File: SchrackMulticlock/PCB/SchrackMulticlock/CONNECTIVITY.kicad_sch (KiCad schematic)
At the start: 26 parts, among them J1 TYPE-C-31-M-12 (USB C CONN), U7 USBLC6-2SC6

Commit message: SchrackMulticlock update
Schematic and PCB update
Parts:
- D4: footprint LED_SMD:LED_Cree-PLCC4_3.2x2.8mm_CCW -> LED_THT:LED_D5.0mm
- D5, D6, D7: footprint LED_SMD:LED_0805_2012Metric_Pad1.15x1.40mm_HandSolder -> LED_THT:LED_D5.0mm
- gave numbers to parts that had none: 2
- renumbered C9 to C10, R9 to R10, R10 to R11, R11 to R12, R5 to R6, R6 to R7, R7 to R8, R8 to R9
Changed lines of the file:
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@@
 			)
 		)
-		(property "Footprint" "LED_SMD:LED_0805_2012Metric_Pad1.15x1.40mm_HandSolder"
+		(property "Footprint" "LED_THT:LED_D5.0mm"
 			(at 217.17 121.92 0)
 			(effects
@@
 		(dnp no)
 		(fields_autoplaced yes)
-		(property "Reference" "#PWR0120"
+		(property "Reference" "#PWR022"
 			(at 173.99 62.23 0)
 			(effects
@@
 			(project "SchrackCounter"
 				(path "/d96f2ffc-3f4c-4f71-b693-29f6b8c3245d/301b3ab9-8372-40d2-93c7-cd7607d23fc4"
-					(reference "#PWR0120")
+					(reference "#PWR022")
 					(unit 1)
 				)
@@
 			)
 		)
-		(property "Footprint" "LED_SMD:LED_0805_2012Metric_Pad1.15x1.40mm_HandSolder"
+		(property "Footprint" "LED_THT:LED_D5.0mm"
 			(at 217.17 135.89 0)
 			(effects
@@
 		(dnp no)
 		(fields_autoplaced yes)
-		(property "Reference" "#PWR0118"
+		(property "Reference" "#PWR024"
 			(at 224.79 132.08 0)
 			(effects
@@
 			(project "SchrackMulticlock"
 				(path "/d96f2ffc-3f4c-4f71-b693-29f6b8c3245d/301b3ab9-8372-40d2-93c7-cd7607d23fc4"
-					(reference "#PWR0118")
+					(reference "#PWR024")
 					(unit 1)
 				)
@@
 		(dnp no)
 		(fields_autoplaced yes)
-		(property "Reference" "#PWR0121"
+		(property "Reference" "#PWR021"
 			(at 179.07 142.24 0)
 			(effects
@@
 			(project "SchrackCounter"
 				(path "/d96f2ffc-3f4c-4f71-b693-29f6b8c3245d/301b3ab9-8372-40d2-93c7-cd7607d23fc4"
-					(reference "#PWR0121")
+					(reference "#PWR021")
 					(unit 1)
 				)
@@
 		(dnp no)
 		(fields_autoplaced yes)
-		(property "Reference" "#PWR0122"
+		(property "Reference" "#PWR020"
 			(at 179.07 128.27 0)
 			(effects
@@
 			(project "SchrackCounter"
 				(path "/d96f2ffc-3f4c-4f71-b693-29f6b8c3245d/301b3ab9-8372-40d2-93c7-cd7607d23fc4"
-					(reference "#PWR0122")
+					(reference "#PWR020")
 					(unit 1)
 				)
@@
 		(dnp no)
 		(fields_autoplaced yes)
-		(property "Reference" "#PWR0113"
+		(property "Reference" "#PWR017"
 			(at 121.92 85.09 0)
 			(effects
@@
 			(project "SchrackCounter"
 				(path "/d96f2ffc-3f4c-4f71-b693-29f6b8c3245d/301b3ab9-8372-40d2-93c7-cd7607d23fc4"
-					(reference "#PWR0113")
+					(reference "#PWR017")
 					(unit 1)
 				)
@@
 		(on_board yes)
 		(dnp no)
-		(property "Reference" "#PWR0123"
+		(property "Reference" "#PWR019"
 			(at 160.02 121.92 0)
 			(effects
@@
 			(project "SchrackCounter"
 				(path "/d96f2ffc-3f4c-4f71-b693-29f6b8c3245d/301b3ab9-8372-40d2-93c7-cd7607d23fc4"
-					(reference "#PWR0123")
+					(reference "#PWR019")
 					(unit 1)
 				)
@@
 		(on_board yes)
 		(dnp no)
-		(property "Reference" "R9"
+		(property "Reference" "R10"
 			(at 173.99 72.39 90)
 			(effects
@@
 			(project "SchrackCounter"
 				(path "/d96f2ffc-3f4c-4f71-b693-29f6b8c3245d/301b3ab9-8372-40d2-93c7-cd7607d23fc4"
-					(reference "R9")
+					(reference "R10")
 					(unit 1)
 				)
@@
 		(dnp no)
 		(fields_autoplaced yes)
-		(property "Reference" "#PWR0117"
+		(property "Reference" "#PWR025"
 			(at 224.79 156.21 0)
 			(effects
@@
 			(project "SchrackMulticlock"
 				(path "/d96f2ffc-3f4c-4f71-b693-29f6b8c3245d/301b3ab9-8372-40d2-93c7-cd7607d23fc4"
-					(reference "#PWR0117")
+					(reference "#PWR025")
 					(unit 1)
 				)
@@
 		(on_board yes)
 		(dnp no)
-		(property "Reference" "R5"
+		(property "Reference" "R6"
 			(at 134.62 128.905 0)
 			(effects
@@
 			(project "SchrackCounter"
 				(path "/d96f2ffc-3f4c-4f71-b693-29f6b8c3245d/301b3ab9-8372-40d2-93c7-cd7607d23fc4"
-					(reference "R5")
+					(reference "R6")
 					(unit 1)
 				)
@@
 		(on_board yes)
 		(dnp no)
-		(property "Reference" "C?"
+		(property "Reference" "C9"
 			(at 113.03 72.39 0)
 			(effects
@@
 			(project "SchrackMulticlock"
 				(path "/d96f2ffc-3f4c-4f71-b693-29f6b8c3245d/301b3ab9-8372-40d2-93c7-cd7607d23fc4"
-					(reference "C?")
+					(reference "C9")
 					(unit 1)
 				)
@@
 		(dnp no)
 		(fields_autoplaced yes)
-		(property "Reference" "#PWR0124"
+		(property "Reference" "#PWR018"
 			(at 142.24 142.24 0)
 			(effects
@@
 			(project "SchrackCounter"
 				(path "/d96f2ffc-3f4c-4f71-b693-29f6b8c3245d/301b3ab9-8372-40d2-93c7-cd7607d23fc4"
-					(reference "#PWR0124")
+					(reference "#PWR018")
 					(unit 1)
 				)
@@
 		(on_board yes)
 		(dnp no)
-		(property "Reference" "R8"
+		(property "Reference" "R9"
 			(at 173.99 46.99 90)
 			(effects
@@
 			(project "SchrackCounter"
 				(path "/d96f2ffc-3f4c-4f71-b693-29f6b8c3245d/301b3ab9-8372-40d2-93c7-cd7607d23fc4"
-					(reference "R8")
+					(reference "R9")
 					(unit 1)
 				)
@@
 		(on_board yes)
 		(dnp no)
-		(property "Reference" "#PWR0115"
+		(property "Reference" "#PWR014"
 			(at 87.63 139.7 0)
 			(effects
@@
 			(project "SchrackCounter"
 				(path "/d96f2ffc-3f4c-4f71-b693-29f6b8c3245d/301b3ab9-8372-40d2-93c7-cd7607d23fc4"
-					(reference "#PWR0115")
+					(reference "#PWR014")
 					(unit 1)
 				)
@@
 		(on_board yes)
 		(dnp no)
-		(property "Reference" "R11"
+		(property "Reference" "R12"
 			(at 201.93 136.525 90)
 			(effects
@@
 			(project "SchrackMulticlock"
 				(path "/d96f2ffc-3f4c-4f71-b693-29f6b8c3245d/301b3ab9-8372-40d2-93c7-cd7607d23fc4"
-					(reference "R11")
+					(reference "R12")
 					(unit 1)
 				)
@@
 		(on_board yes)
 		(dnp no)
-		(property "Reference" "R?"
+		(property "Reference" "R5"
 			(at 105.41 72.39 0)
 			(effects
@@
 			(project "SchrackMulticlock"
 				(path "/d96f2ffc-3f4c-4f71-b693-29f6b8c3245d/301b3ab9-8372-40d2-93c7-cd7607d23fc4"
-					(reference "R?")
+					(reference "R5")
 					(unit 1)
 				)
@@
 		(on_board yes)
 		(dnp no)
-		(property "Reference" "#PWR0116"
+		(property "Reference" "#PWR013"
 			(at 87.63 127 0)
 			(effects
@@
 			(project "SchrackCounter"
 				(path "/d96f2ffc-3f4c-4f71-b693-29f6b8c3245d/301b3ab9-8372-40d2-93c7-cd7607d23fc4"
-					(reference "#PWR0116")
+					(reference "#PWR013")
 					(unit 1)
 				)
@@
 		(on_board yes)
 		(dnp no)
-		(property "Reference" "#PWR0114"
+		(property "Reference" "#PWR015"
 			(at 87.63 151.13 0)
 			(effects
@@
 			(project "SchrackCounter"
 				(path "/d96f2ffc-3f4c-4f71-b693-29f6b8c3245d/301b3ab9-8372-40d2-93c7-cd7607d23fc4"
-					(reference "#PWR0114")
+					(reference "#PWR015")
 					(unit 1)
 				)
@@
 			)
 		)
-		(property "Footprint" "LED_SMD:LED_0805_2012Metric_Pad1.15x1.40mm_HandSolder"
+		(property "Footprint" "LED_THT:LED_D5.0mm"
 			(at 217.17 146.05 0)
 			(effects
@@
 		(on_board yes)
 		(dnp no)
-		(property "Reference" "R6"
+		(property "Reference" "R7"
 			(at 172.72 117.475 90)
 			(effects
@@
 			(project "SchrackCounter"
 				(path "/d96f2ffc-3f4c-4f71-b693-29f6b8c3245d/301b3ab9-8372-40d2-93c7-cd7607d23fc4"
-					(reference "R6")
+					(reference "R7")
 					(unit 1)
 				)
@@
 		(on_board yes)
 		(dnp no)
-		(property "Reference" "C9"
+		(property "Reference" "C10"
 			(at 227.33 66.04 0)
 			(effects
@@
 			(project "SchrackCounter"
 				(path "/d96f2ffc-3f4c-4f71-b693-29f6b8c3245d/301b3ab9-8372-40d2-93c7-cd7607d23fc4"
-					(reference "C9")
+					(reference "C10")
 					(unit 1)
 				)
@@
 		(dnp no)
 		(fields_autoplaced yes)
-		(property "Reference" "#PWR01"
+		(property "Reference" "#PWR016"
 			(at 118.11 85.09 0)
 			(effects
@@
 			(project "SchrackMulticlock"
 				(path "/d96f2ffc-3f4c-4f71-b693-29f6b8c3245d/301b3ab9-8372-40d2-93c7-cd7607d23fc4"
-					(reference "#PWR01")
+					(reference "#PWR016")
 					(unit 1)
 				)
@@
 		(dnp no)
 		(fields_autoplaced yes)
-		(property "Reference" "#PWR0119"
+		(property "Reference" "#PWR023"
 			(at 223.52 76.2 0)
 			(effects
@@
 			(project "SchrackCounter"
 				(path "/d96f2ffc-3f4c-4f71-b693-29f6b8c3245d/301b3ab9-8372-40d2-93c7-cd7607d23fc4"
-					(reference "#PWR0119")
+					(reference "#PWR023")
 					(unit 1)
 				)
@@
 		(on_board yes)
 		(dnp no)
-		(property "Reference" "R7"
+		(property "Reference" "R8"
 			(at 172.72 131.445 90)
 			(effects
@@
 			(project "SchrackCounter"
 				(path "/d96f2ffc-3f4c-4f71-b693-29f6b8c3245d/301b3ab9-8372-40d2-93c7-cd7607d23fc4"
-					(reference "R7")
+					(reference "R8")
 					(unit 1)
 				)
@@
 		(on_board yes)
 		(dnp no)
-		(property "Reference" "R10"
+		(property "Reference" "R11"
 			(at 201.93 112.395 90)
 			(effects
@@
 			(project "SchrackMulticlock"
 				(path "/d96f2ffc-3f4c-4f71-b693-29f6b8c3245d/301b3ab9-8372-40d2-93c7-cd7607d23fc4"
-					(reference "R10")
+					(reference "R11")
 					(unit 1)
 				)
@@
 			)
 		)
-		(property "Footprint" "LED_SMD:LED_Cree-PLCC4_3.2x2.8mm_CCW"
+		(property "Footprint" "LED_THT:LED_D5.0mm"
 			(at 217.17 111.76 0)
 			(effects
@@
 			)
 		)
-		(property "Datasheet" "~"
+		(property "Datasheet" "https://cz.mouser.com/ProductDetail/Cree-LED/CLM2B-REW-CYaZ0AA3?qs=3AcK5DacLboBP3rYC%2FbEBg%3D%3D"
 			(at 217.17 111.76 0)
 			(effects

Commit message: SchrackCounter update - FIX
USB footprint standoff fix
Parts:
- J1: footprint sumec_brd:USB_Type_C -> Connector_USB:USB_C_Receptacle_GCT_USB4105-xx-A_16P_TopMnt_Horizontal
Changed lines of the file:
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@@
 			)
 		)
-		(property "Footprint" "sumec_brd:USB_Type_C"
+		(property "Footprint" "Connector_USB:USB_C_Receptacle_GCT_USB4105-xx-A_16P_TopMnt_Horizontal"
 			(at 146.05 62.23 0)
 			(effects

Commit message: Multiclock pcb update
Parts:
- J1: footprint Connector_USB:USB_C_Receptacle_GCT_USB4105-xx-A_16P_TopMnt_Horizontal -> sumec_brd:HRO_TYPE-C-31-M-12
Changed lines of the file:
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@@
 			)
 		)
-		(property "Footprint" "Connector_USB:USB_C_Receptacle_GCT_USB4105-xx-A_16P_TopMnt_Horizontal"
+		(property "Footprint" "sumec_brd:HRO_TYPE-C-31-M-12"
 			(at 146.05 62.23 0)
 			(effects

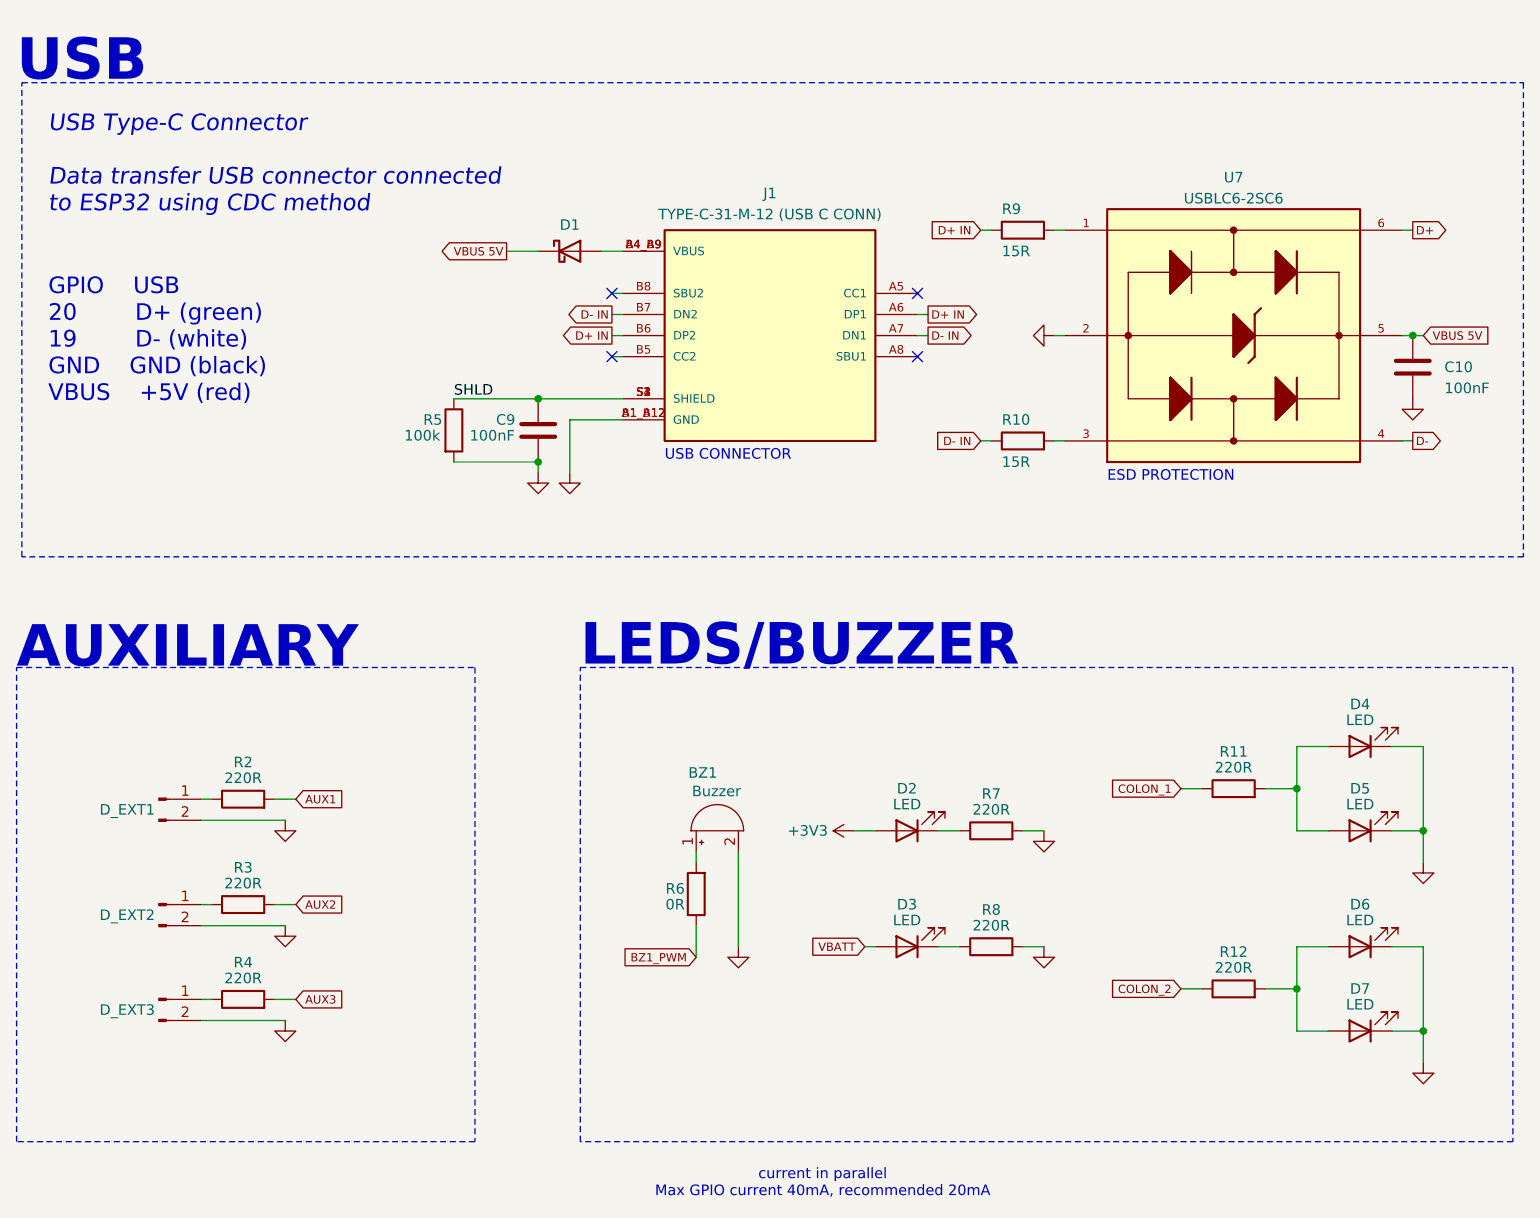
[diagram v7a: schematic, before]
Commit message: SchrackMulticlock and Counter pcb updates
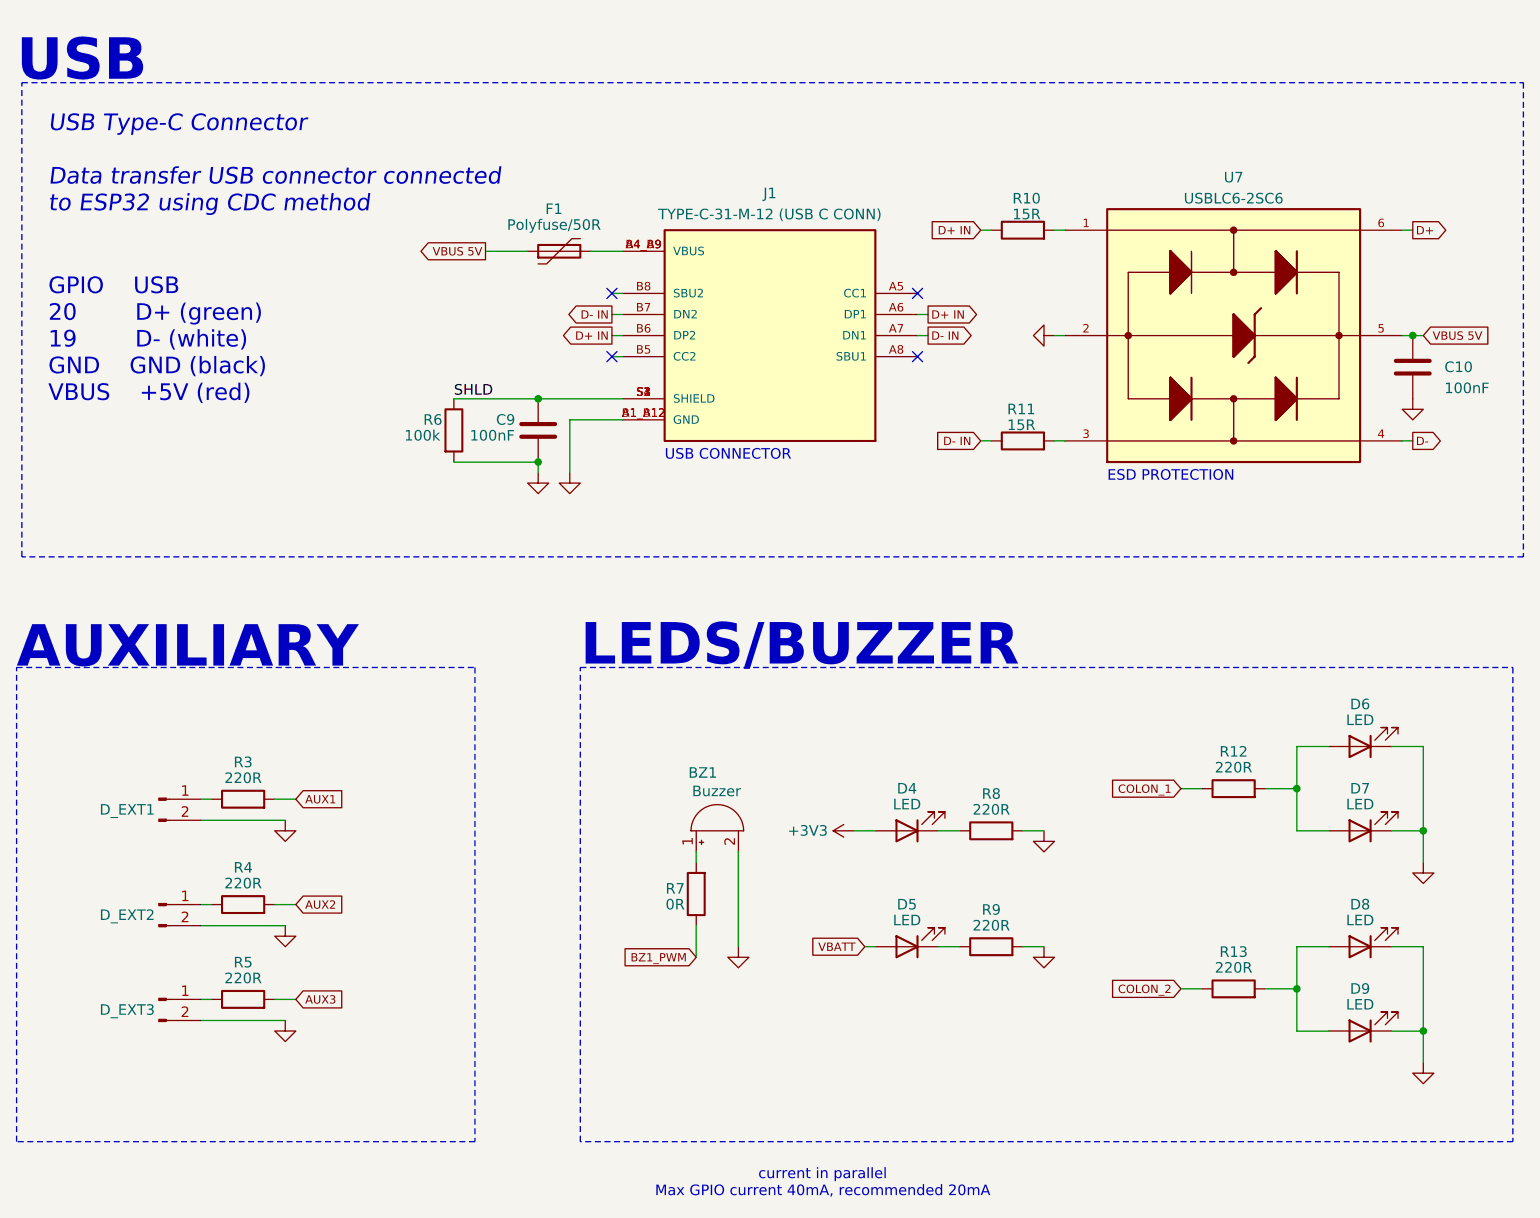
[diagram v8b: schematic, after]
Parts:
- removed D1: D_Schottky, Diode_SMD:D_1206_3216Metric_Pad1.42x1.75mm_HandSolder, symbol Device:D_Schottky
- added F1: Polyfuse/50R, Fuse:Fuse_0805_2012Metric, symbol Device:Polyfuse
- renumbered D2 to D4, D3 to D5, D4 to D6, D5 to D7, D6 to D8, D7 to D9, R9 to R10, R10 to R11, R11 to R12, R12 to R13, R2 to R3, R3 to R4, R4 to R5, R5 to R6, R6 to R7, R7 to R8, R8 to R9
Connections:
- net VBUS 5V: now also F1.1
- net at J1.A4_B9 (VBUS), J1.B4_A9 (VBUS): now also F1.2
